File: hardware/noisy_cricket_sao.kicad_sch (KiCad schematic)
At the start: 0 parts

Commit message: Create part symbols, working on schematic.
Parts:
- added C1, C4: 0.39uF, Capacitor_SMD:C_0402_1005Metric, symbol Device:C
- added C2, C3, C5: 1uF, Capacitor_SMD:C_0402_1005Metric, symbol Device:C
- added DS1: E6CC1205RGBC3UDA, symbol noisy_cricket_sao:E6CC1205RGBC3UDA
- added J1: Debug Pogo 6-Pin, symbol noisy_cricket_sao:Debug Pogo 6-Pin
- added J2: SAO 6-Pin, symbol noisy_cricket_sao:SAO_6-Pin
- added MIC1: LMD3526B261-OA5, symbol noisy_cricket_sao:LMD3526B261-OA5
- added R1: 100, Resistor_SMD:R_0402_1005Metric, symbol Device:R_US
- added R2, R3: 0, Resistor_SMD:R_0402_1005Metric, symbol Device:R_US
- added R4, R7: 20k, Resistor_SMD:R_0402_1005Metric, symbol Device:R_US
- added R6: 68k, Resistor_SMD:R_0402_1005Metric, symbol Device:R_US
- added SPK1: 1510-8Ω1W-L60MM, symbol noisy_cricket_sao:1510-8Ω1W-L60MM
- added U1: AD8107, symbol noisy_cricket_sao:AD8107
- added U2: CH32V003F4U6, symbol noisy_cricket_sao:CH32V003F4U6
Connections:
- new net: DS1.4 (BK), R3.2
- new net: C2.2, U1.2 (BYPASS), U1.3 (INP)
- new net: R6.1, R7.2, U1.4 (INN)
- new net: R6.2, SPK1.1 (+), U1.5 (VO1)
- new net: SPK1.2 (-), U1.8 (VO2)
- new net: DS1.3 (GK), R2.2
- new net: DS1.1 (RK), R1.2
- new net: C1.2, R7.1
- new net +3V3: C3.1, C4.2, C5.2, DS1.2 (A), J1.1 (VDD), J2.1 (VDD), MIC1.4 (VDD), R4.1, U1.6 (VDD), U2.6 (VDD)
- new net AMP_SD: U1.1 (SD)
- new net AUDIO: C1.1
- new net GND: C2.1, C3.2, C4.1, C5.1, J1.6 (GND), J2.2 (GND), MIC1.2 (L/R), MIC1.5 (GND), U1.7 (GND), U2.4 (GND), U2.EP (GND)
- new net LED_B: R3.1
- new net LED_G: R2.1
- new net LED_R: R1.1
- new net PDM_CLK: MIC1.3 (CLK)
- new net PDM_DATA: MIC1.1 (DATA)
- new net RESET: J1.2 (RESET), U2.1 (PD7_NRST)
- new net SCL: J2.4 (SCL)
- new net SDA: J2.3 (SDA)
- new net SWIO: J1.3 (SWDIO), R4.2, U2.15 (PD1_SWIO)
- new net UART: J1.5 (UART)
- no-connect marks 0 -> 3

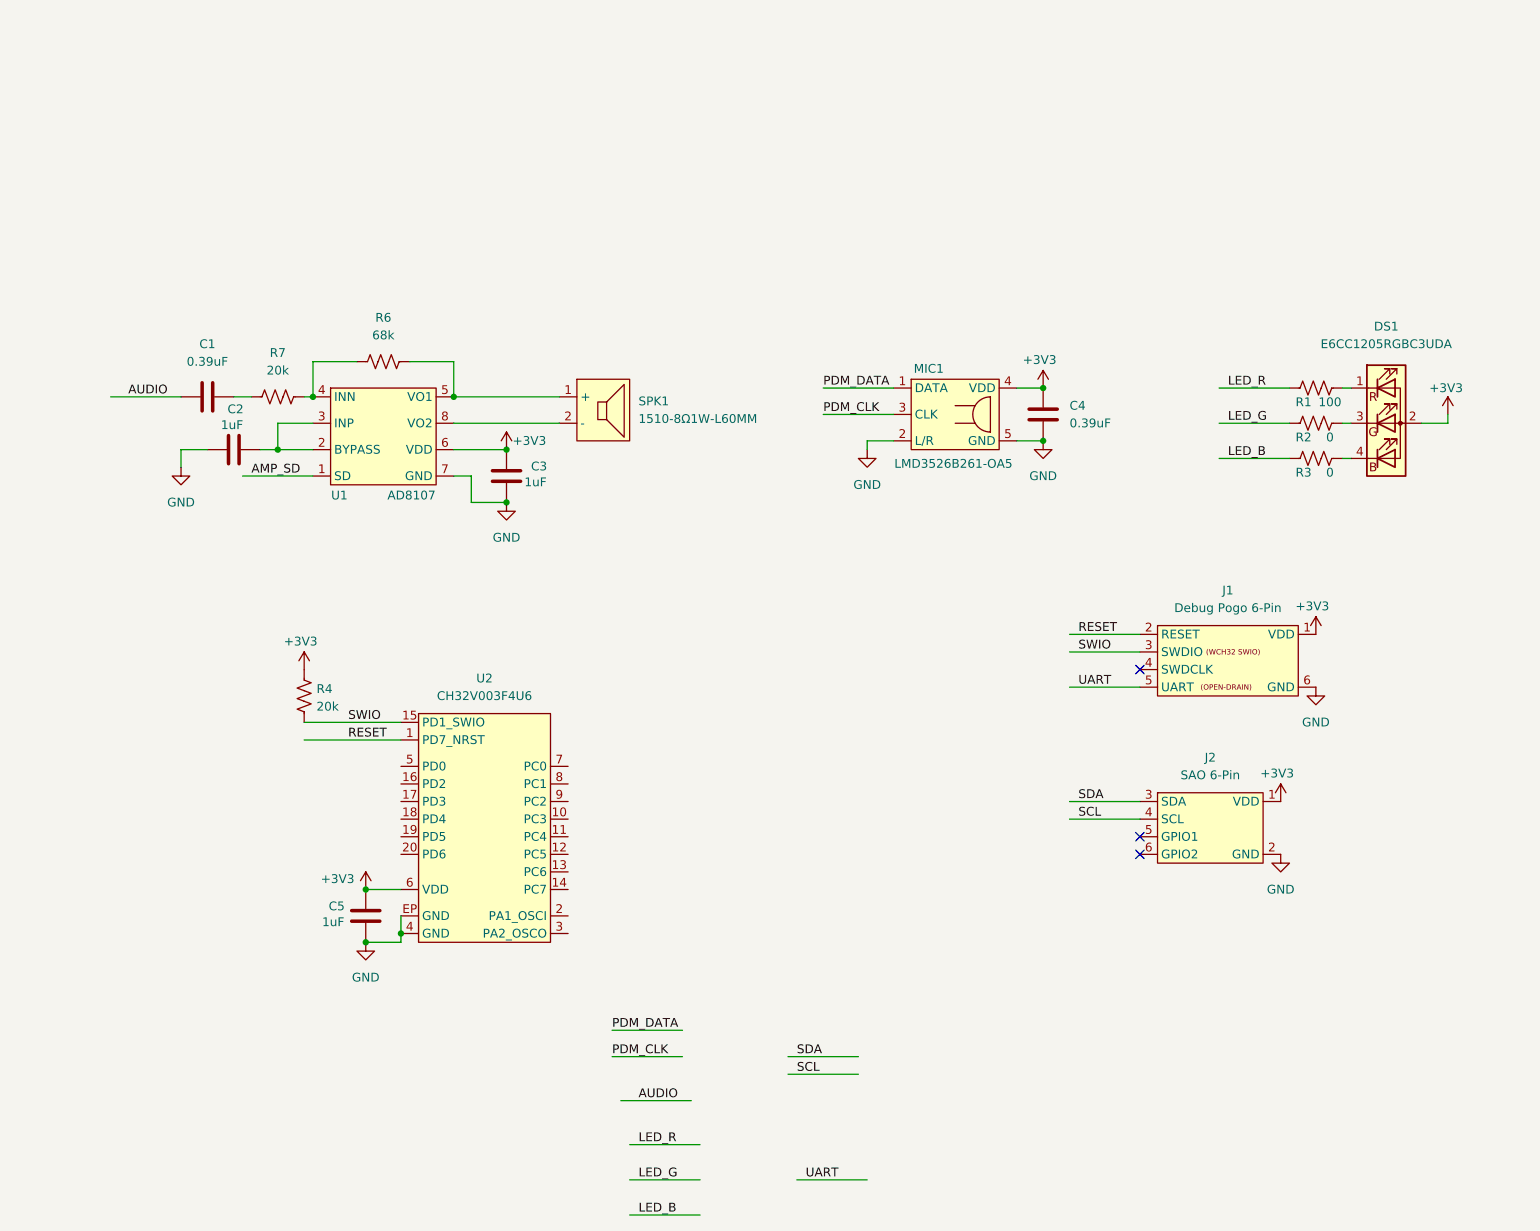
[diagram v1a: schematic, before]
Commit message: Finish schematic
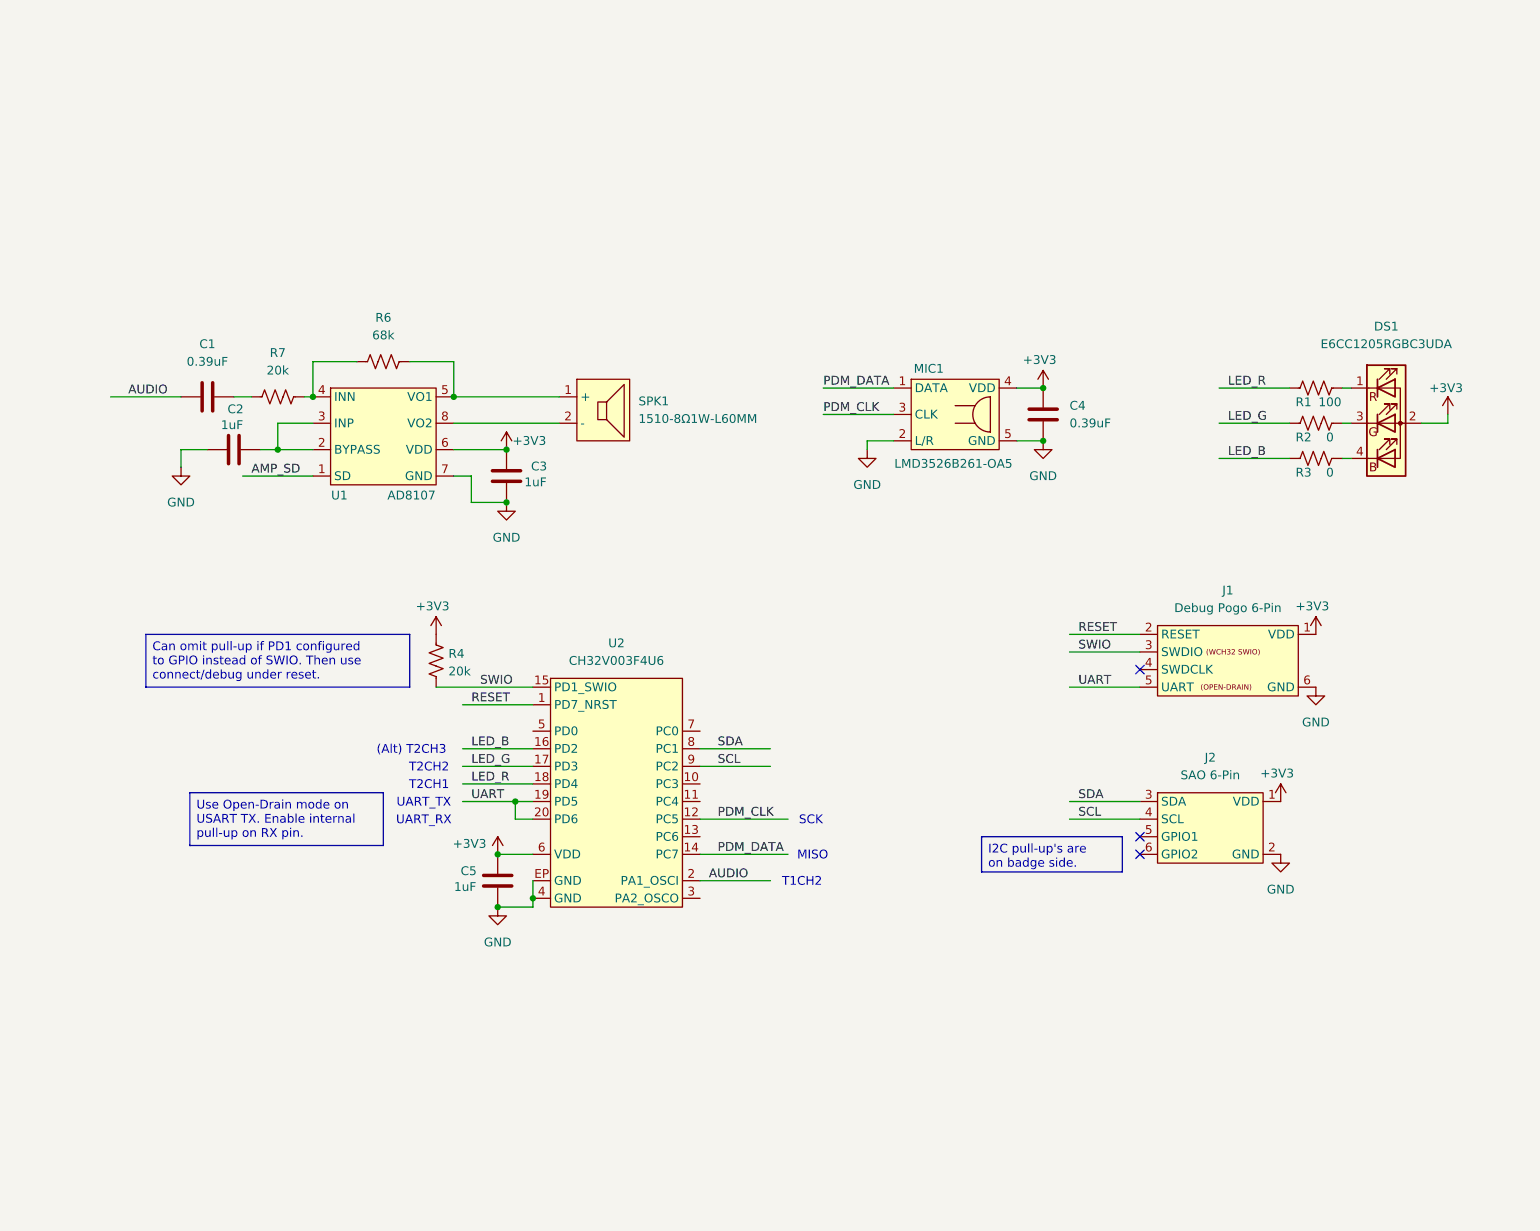
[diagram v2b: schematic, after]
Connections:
- net AUDIO: now also U2.2 (PA1_OSCI)
- net LED_B: now also U2.16 (PD2)
- net LED_G: now also U2.17 (PD3)
- net LED_R: now also U2.18 (PD4)
- net PDM_CLK: now also U2.12 (PC5)
- net PDM_DATA: now also U2.14 (PC7)
- net SCL: now also U2.9 (PC2)
- net SDA: now also U2.8 (PC1)
- net UART: now also U2.19 (PD5), U2.20 (PD6)
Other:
- note added: "(Alt) T2CH3"
- note added: "MISO"
- note added: "SCK"
- note added: "T1CH2"
- note added: "T2CH1"
- note added: "T2CH2"
- note added: "UART_RX"
- note added: "UART_TX"
- title: (none) -> Noisy Cricket SAO 2026
- moved on the sheet: C5, R4, U2

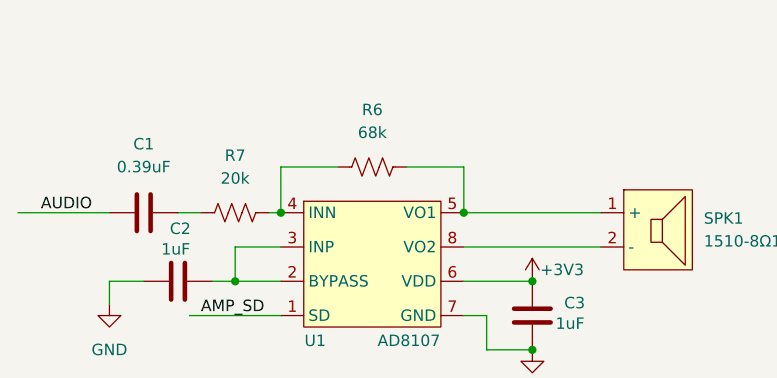
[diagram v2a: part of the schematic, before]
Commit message: Create empty footprints, add low pass filter to amp
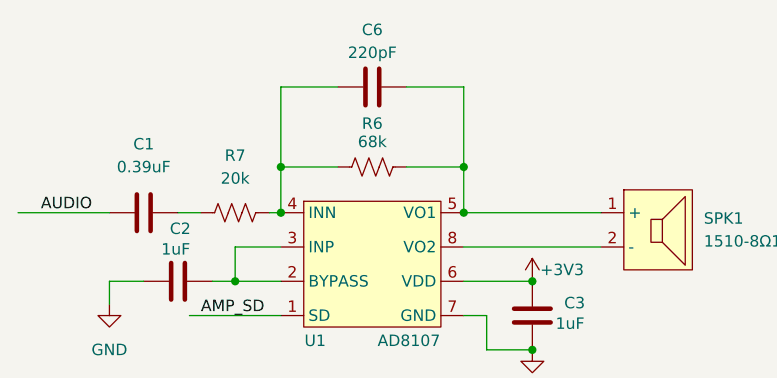
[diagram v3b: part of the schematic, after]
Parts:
- added C6: 220pF, Capacitor_SMD:C_0402_1005Metric, symbol Device:C
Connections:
- net at R6.1, R7.2, U1.4 (INN): now also C6.1
- net at R6.2, SPK1.1 (+), U1.5 (VO1): now also C6.2
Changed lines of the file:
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@@
+	)
+	(junction
+		(at 86.36 63.5)
+		(diameter 0)
+		(color 0 0 0 0)
 	)
 	(junction
@@
 	)
 	(junction
+		(at 66.04 63.5)
+		(diameter 0)
+		(color 0 0 0 0)
+	)
+	(junction
 		(at 93.98 83.82)
 		(diameter 0)
@@
 	(wire
 		(pts
+			(xy 66.04 54.61) (xy 66.04 63.5)
+		)
+		(stroke
+			(width 0)
+			(type default)
+		)
+	)
+	(wire
+		(pts
 			(xy 121.92 119.38) (xy 132.08 119.38)
 		)
@@
 	(wire
 		(pts
+			(xy 86.36 54.61) (xy 86.36 63.5)
+		)
+		(stroke
+			(width 0)
+			(type default)
+		)
+	)
+	(wire
+		(pts
 			(xy 87.63 121.92) (xy 97.79 121.92)
 		)
@@
 	(wire
 		(pts
+			(xy 72.39 54.61) (xy 66.04 54.61)
+		)
+		(stroke
+			(width 0)
+			(type default)
+		)
+	)
+	(wire
+		(pts
 			(xy 196.85 77.47) (xy 207.01 77.47)
 		)
@@
 		(pts
 			(xy 97.79 129.54) (xy 95.25 129.54)
+		)
+		(stroke
+			(width 0)
+			(type default)
+		)
+	)
+	(wire
+		(pts
+			(xy 80.01 54.61) (xy 86.36 54.61)
 		)
 		(stroke
@@
 		(on_board yes)
 		(dnp no)
-		(fields_autoplaced yes)
 		(property "Reference" "R6"
-			(at 76.2 57.15 90)
+			(at 76.2 58.674 90)
 			(effects
 				(font
@@
 		)
 		(property "Value" "68k"
-			(at 76.2 59.69 90)
+			(at 76.2 60.706 90)
 			(effects
 				(font
@@
 					(unit 1)
 				)
+			)
+		)
+	)
+	(symbol
+		(lib_id "Device:C")
+		(at 76.2 54.61 90)
+		(unit 1)
+		(exclude_from_sim no)
+		(in_bom yes)
+		(on_board yes)
+		(dnp no)
+		(property "Reference" "C6"
+			(at 76.2 48.26 90)
+			(effects
+				(font
+					(size 1.27 1.27)
+				)
+			)
+		)
+		(property "Value" "220pF"
+			(at 76.2 50.8 90)
+			(effects
+				(font
+					(size 1.27 1.27)
+				)
+			)
+		)
+		(property "Footprint" "Capacitor_SMD:C_0402_1005Metric"
+			(at 80.01 53.6448 0)
+			(effects
+				(font
+					(size 1.27 1.27)
+				)
+				(hide yes)
+			)
+		)
+		(property "Datasheet" "~"
+			(at 76.2 54.61 0)
+			(effects
+				(font
+					(size 1.27 1.27)
+				)
+				(hide yes)
+			)
+		)
+		(property "Description" "Unpolarized capacitor"
+			(at 76.2 54.61 0)
+			(effects
+				(font
+					(size 1.27 1.27)
+				)
+				(hide yes)
+			)
+		)
+		(pin "2"
+		)
+		(pin "1"
+		)
+		(instances
+			(project "noisy_cricket_sao"
+				(path "/3f7eb731-322c-463d-a9ad-01b80ab04f9c"
+					(reference "C6")
+					(unit 1)
+				)
